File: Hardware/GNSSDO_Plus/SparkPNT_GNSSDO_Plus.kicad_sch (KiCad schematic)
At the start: 52 parts, among them J7 Qwiic_Vertical, J9 Screw_Cage_3.5mm-10, U1 ESP32-WROVER-IE-N16R8, U18 MS8607-02BA

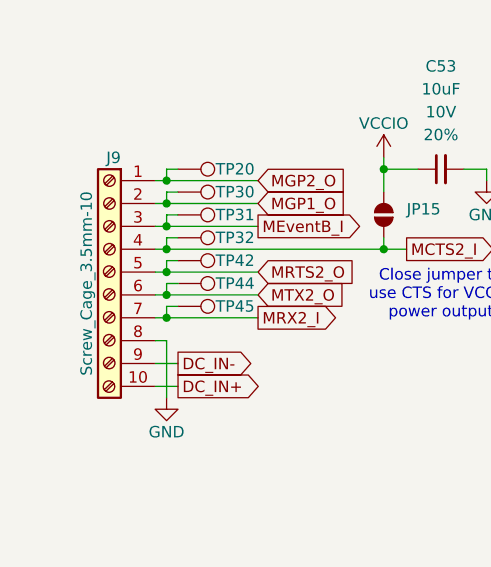
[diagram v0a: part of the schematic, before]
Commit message: Update GNSSDO KiCad files to match latest SparkFun library
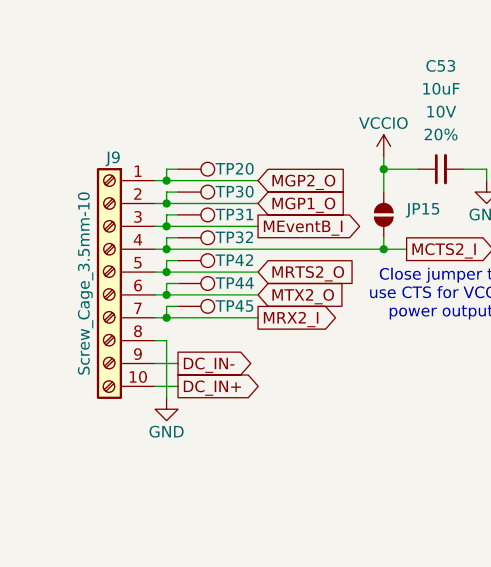
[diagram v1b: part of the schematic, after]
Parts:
- C1: PROD_ID CAP-11015 -> CAP-25001
- C54: PROD_ID CAP-07888 -> CAP-24999
- J7: footprint SparkFun-Connector:JST_SMD_1.0mm-4_Vertical_Black -> SparkFun-Connector:JST_1x04_P1.0mm_Vertical_SMD
- J9: footprint SparkFun-Connector:Screw_Cage_3.5mm-10 -> SparkFun-Connector:ScrewCage_1x10_P3.5mm_Horizontal; symbol SparkFun-Connector:Screw_Cage_3.5mm-10 -> SparkFun-Connector:ScrewCage_1x10_P3.5mm_Green
- TP24, TP25, TP26, TP43: footprint SparkFun-Connector:1x01 -> SparkFun-Connector:1x01_P2.54mm
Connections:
- net at J7.NC1 (NC): no longer J7.NC2 (NC)
